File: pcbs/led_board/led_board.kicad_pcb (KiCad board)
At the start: 2 copper layers, 22 x 16.5 mm, 6 parts, among them J1 CONN HEADER R/A 2POS 1.5MM, U1 1.4-40V PWM Dimmer 100mA

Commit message: update led board to version 1.0 (just text upates)
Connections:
- R1 pad 1: unconnected-(R1-Pad1) -> Net-(U1-REXT)
- R1 pad 2: unconnected-(R1-Pad2) -> +5V
- U1 pad 6: unconnected-(U1-REXT-Pad6) -> Net-(U1-REXT)
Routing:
- net Net-(U1-REXT): track 0.00 -> 12.7 mm
- net (no net): track 12.7 -> 0.00 mm
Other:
- board text added: "GEOM.KOPFLAB.ORG"

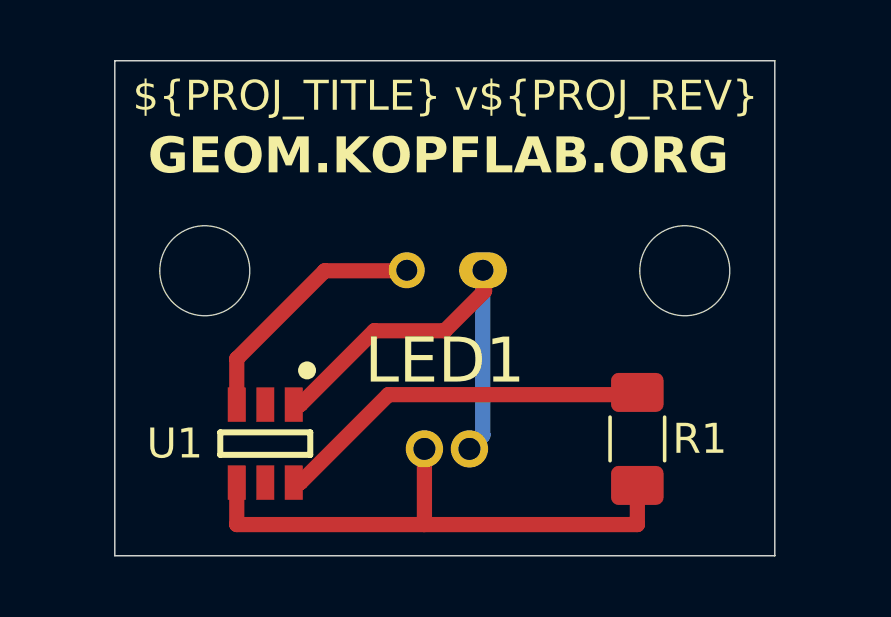
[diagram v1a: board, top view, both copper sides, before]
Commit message: update LED board with multiple resistor options
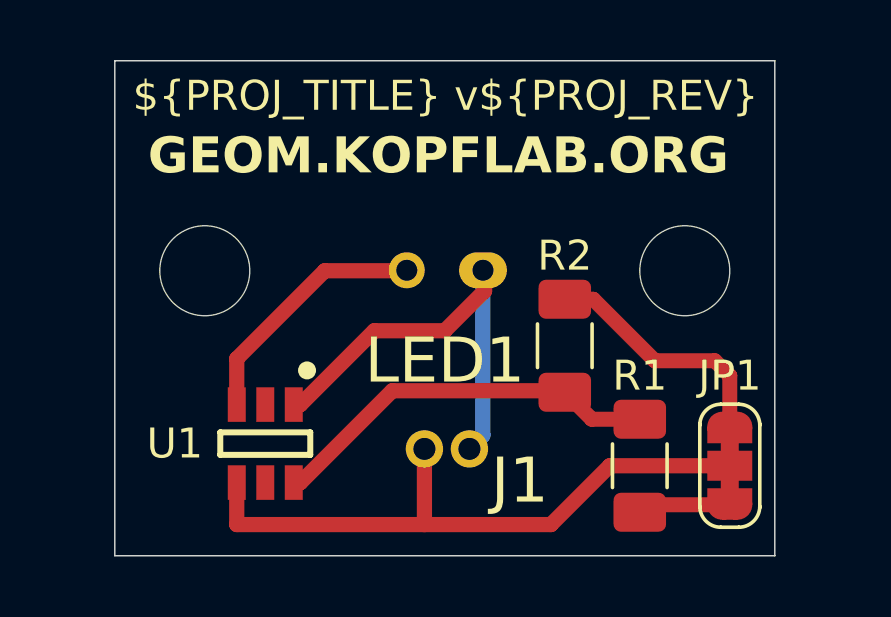
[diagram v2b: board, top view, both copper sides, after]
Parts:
- added JP1: SolderJumper_3_Bridged123, footprints:SolderJumper3_Bridged, F.Cu at (165.5, 108.5)
- added R2: 56Ω, footprints:R_1206, F.Cu at (160.0, 104.5)
- R1: value 47Ω -> 22Ω
- moved R1 0.90 mm to (162.5, 108.5)
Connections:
- R1 pad 2: +5V -> Net-(JP1-B)
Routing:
- net Net-(JP1-A): track 0.00 -> 8.26 mm
- net Net-(JP1-B): track 0.00 -> 3.60 mm
- net +5V: track 18.7 -> 21.2 mm
- net Net-(U1-REXT): track 12.7 -> 14.1 mm
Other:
- board text added: "anode"
- board text added: "cathode"
